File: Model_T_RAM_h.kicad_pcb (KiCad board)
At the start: 2 copper layers, 19.8 x 34.3 mm, 4 parts, among them J1 KC-85_RAM, U1 6264, U2 74HC86

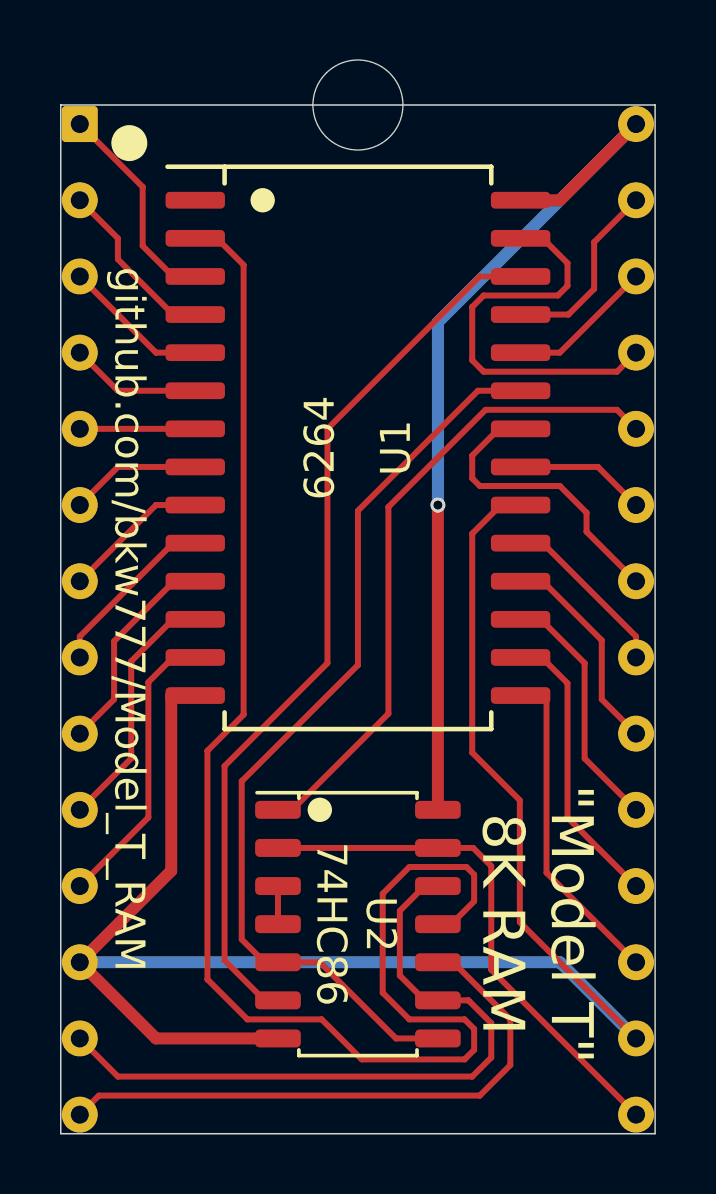
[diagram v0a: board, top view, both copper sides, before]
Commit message: RAM_RST on /CE instead of /OE
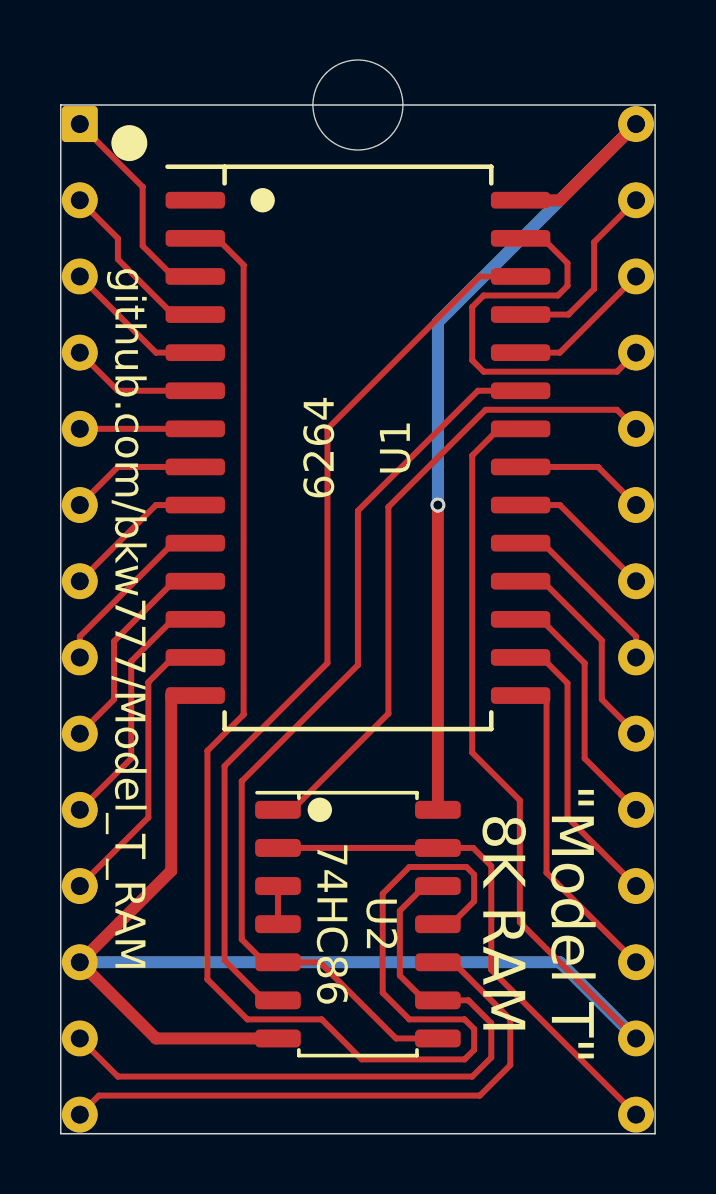
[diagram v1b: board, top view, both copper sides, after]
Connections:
- J1 pad 22: /~OE -> /RAM_RST
- U1 pad 20: GND -> /RAM_RST
- U1 pad 22: /~OE -> GND
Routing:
- net /~OE: track 10.00 -> 0.00 mm
- net /RAM_RST: track 0.00 -> 4.90 mm
- net GND: track 59.3 -> 61.9 mm
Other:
- board text added: "v005 h"
- board text removed: "v004"
